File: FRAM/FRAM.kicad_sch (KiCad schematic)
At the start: 4 parts, among them IC1 MB85RC256VPF-G-JNERE2

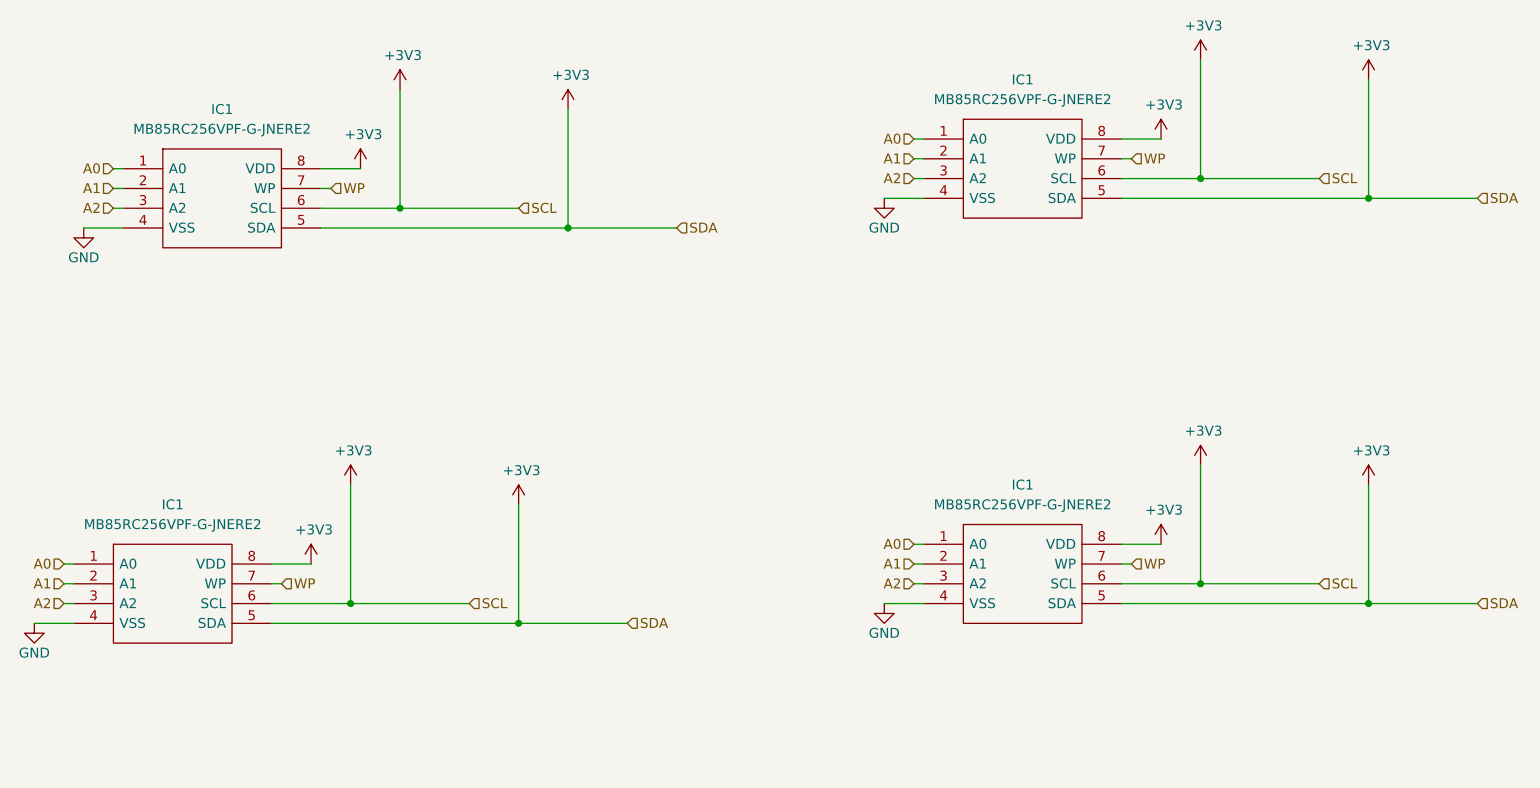
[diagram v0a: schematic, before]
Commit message: Route sensors, IMU and radio board
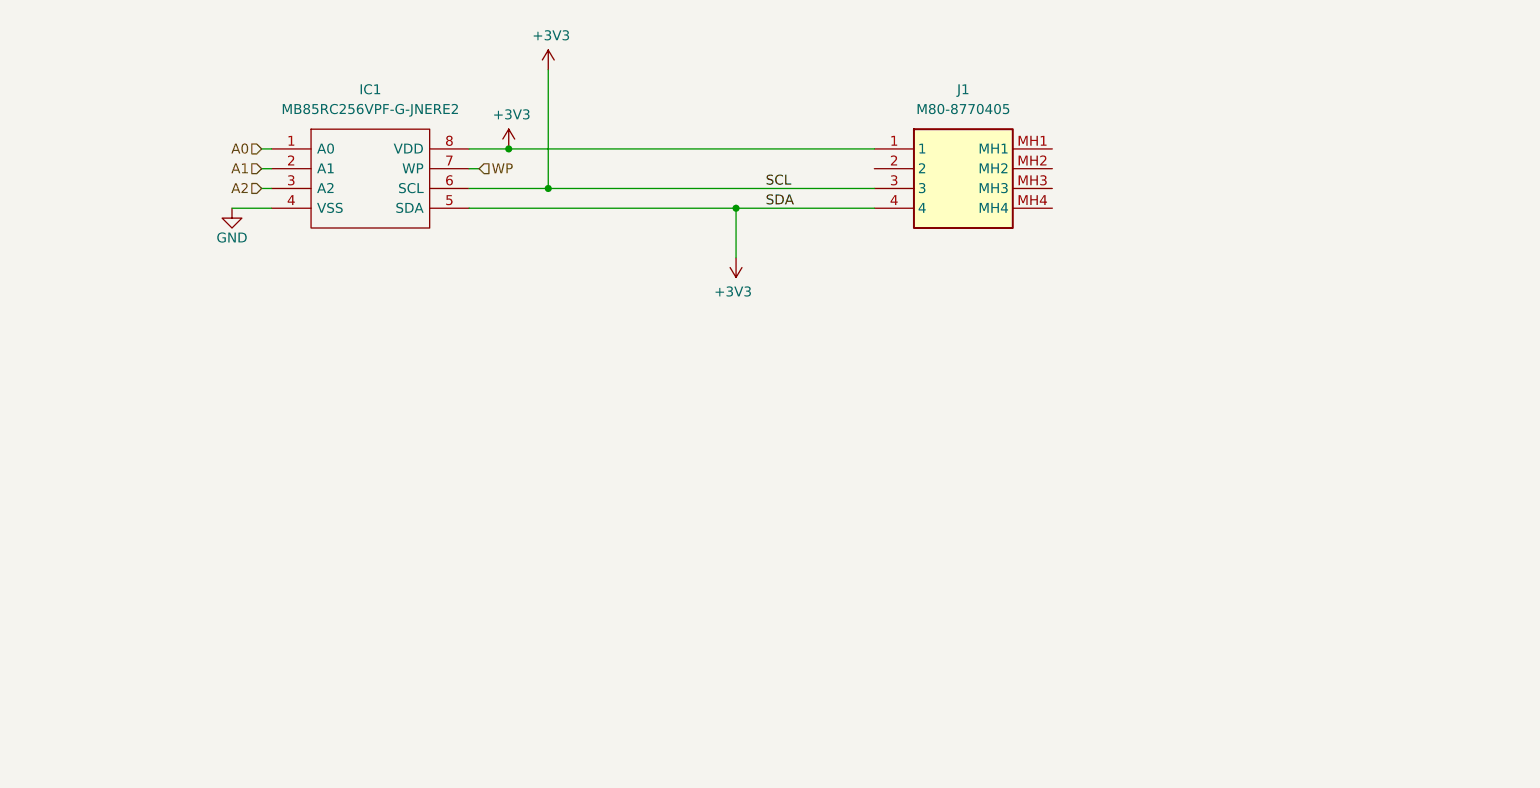
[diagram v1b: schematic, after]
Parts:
- removed IC1 (x3): MB85RC256VPF-G-JNERE2, MB85RC256VPF-G-JNERE2:SOP127P797X210-8N, symbol LibraryLoader:MB85RC256VPF-G-JNERE2
- added J1: M80-8770405, M808770405, symbol M80-8770405:M80-8770405
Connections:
- net +3V3: now also J1.1, J1.3, J1.4
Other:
- moved on the sheet: IC1

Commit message: Done with most of the boards
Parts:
- added R1 (x2): R, Resistor_SMD:R_0603_1608Metric, symbol Device:R
- J1: footprint M808770405 -> KiCad:M808770405
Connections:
- net WP is gone; now on net GND: IC1.7 (WP)
- net +3V3: no longer IC1.5 (SDA), IC1.6 (SCL), J1.3, J1.4
- net GND: now also J1.2
- new net: IC1.6 (SCL), R1.1
- new net SCL: J1.3, R1.2
- new net SDA: IC1.5 (SDA), J1.4, R1.1, R1.2
- no-connect marks 0 -> 4
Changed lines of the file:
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@@
 (kicad_sch (version 20230121) (generator eeschema)
   (paper "A4")
-  (junction (at 147.32 69.85) (diameter 0) (color 0 0 0 0)
-  )
-  (junction (at 123.19 67.31) (diameter 0) (color 0 0 0 0)
+  (junction (at 142.24 69.85) (diameter 0) (color 0 0 0 0)
+  )
+  (junction (at 149.86 69.85) (diameter 0) (color 0 0 0 0)
   )
   (junction (at 118.11 62.23) (diameter 0) (color 0 0 0 0)
   )
+  (junction (at 138.43 64.77) (diameter 0) (color 0 0 0 0)
+  )
+  (no_connect (at 187.96 67.31))
+  (no_connect (at 187.96 64.77))
+  (no_connect (at 187.96 69.85))
+  (no_connect (at 187.96 62.23))
+  (wire (pts (xy 138.43 64.77) (xy 165.1 64.77))
+    (stroke (width 0) (type default))
+  )
   (wire (pts (xy 118.11 62.23) (xy 165.1 62.23))
     (stroke (width 0) (type default))
@@
     (stroke (width 0) (type default))
   )
-  (wire (pts (xy 113.03 64.77) (xy 114.3 64.77))
-    (stroke (width 0) (type default))
-  )
-  (wire (pts (xy 113.03 69.85) (xy 147.32 69.85))
+  (wire (pts (xy 138.43 64.77) (xy 138.43 76.2))
+    (stroke (width 0) (type default))
+  )
+  (wire (pts (xy 113.03 69.85) (xy 142.24 69.85))
     (stroke (width 0) (type default))
   )
@@
     (stroke (width 0) (type default))
   )
+  (wire (pts (xy 86.36 62.23) (xy 87.63 62.23))
+    (stroke (width 0) (type default))
+  )
+  (wire (pts (xy 149.86 69.85) (xy 165.1 69.85))
+    (stroke (width 0) (type default))
+  )
+  (wire (pts (xy 113.03 64.77) (xy 138.43 64.77))
+    (stroke (width 0) (type default))
+  )
+  (wire (pts (xy 130.81 67.31) (xy 165.1 67.31))
+    (stroke (width 0) (type default))
+  )
+  (wire (pts (xy 142.24 69.85) (xy 149.86 69.85))
+    (stroke (width 0) (type default))
+  )
+  (wire (pts (xy 113.03 67.31) (xy 123.19 67.31))
+    (stroke (width 0) (type default))
+  )
+  (wire (pts (xy 86.36 67.31) (xy 87.63 67.31))
+    (stroke (width 0) (type default))
+  )
   (wire (pts (xy 82.55 69.85) (xy 87.63 69.85))
-    (stroke (width 0) (type default))
-  )
-  (wire (pts (xy 123.19 67.31) (xy 165.1 67.31))
-    (stroke (width 0) (type default))
-  )
-  (wire (pts (xy 147.32 69.85) (xy 165.1 69.85))
-    (stroke (width 0) (type default))
-  )
-  (wire (pts (xy 86.36 62.23) (xy 87.63 62.23))
-    (stroke (width 0) (type default))
-  )
-  (wire (pts (xy 123.19 52.07) (xy 123.19 67.31))
-    (stroke (width 0) (type default))
-  )
-  (wire (pts (xy 147.32 69.85) (xy 147.32 76.2))
-    (stroke (width 0) (type default))
-  )
-  (wire (pts (xy 113.03 67.31) (xy 123.19 67.31))
-    (stroke (width 0) (type default))
-  )
-  (wire (pts (xy 86.36 67.31) (xy 87.63 67.31))
     (stroke (width 0) (type default))
   )
@@
   (hierarchical_label "A2" (shape input) (at 86.36 67.31 180) (fields_autoplaced)
     (effects (font (size 1.27 1.27)) (justify right))
-  )
-  (hierarchical_label "WP" (shape input) (at 114.3 64.77 0) (fields_autoplaced)
-    (effects (font (size 1.27 1.27)) (justify left))
   )
   (hierarchical_label "A1" (shape input) (at 86.36 64.77 180) (fields_autoplaced)
@@
     )
   )
-  (symbol (lib_id "power:+3V3") (at 147.32 76.2 180) (unit 1)
+  (symbol (lib_id "power:GND") (at 138.43 76.2 0) (unit 1)
     (in_bom yes) (on_board yes) (dnp no)
-    (property "Reference" "#PWR09" (at 147.32 72.39 0)
-      (effects (font (size 1.27 1.27)) hide)
-    )
-    (property "Value" "+3V3" (at 146.939 80.5942 0)
-      (effects (font (size 1.27 1.27)))
-    )
-    (property "Footprint" "" (at 147.32 76.2 0)
-      (effects (font (size 1.27 1.27)) hide)
-    )
-    (property "Datasheet" "" (at 147.32 76.2 0)
-      (effects (font (size 1.27 1.27)) hide)
-    )
-    (pin "1")
-    (instances
-      (project "STM32F405RGT6-Breakout"
-        (path "/0540e924-c3ed-4064-b360-826f481ae85c"
-          (reference "#PWR09") (unit 1)
-        )
-      )
+    (property "Reference" "#PWR03" (at 138.43 82.55 0)
+      (effects (font (size 1.27 1.27)) hide)
+    )
+    (property "Value" "GND" (at 138.43 80.01 0)
+      (effects (font (size 1.27 1.27)))
+    )
+    (property "Footprint" "" (at 138.43 76.2 0)
+      (effects (font (size 1.27 1.27)) hide)
+    )
+    (property "Datasheet" "" (at 138.43 76.2 0)
+      (effects (font (size 1.27 1.27)) hide)
+    )
+    (pin "1")
+    (instances
       (project "Flight_Computer_V2"
         (path "/39d7ebb3-b69d-4ae9-8f55-c9acfe77d345/4a05f57f-ad7d-4317-b08f-5601038a99f3"
-          (reference "#PWR09") (unit 1)
+          (reference "#PWR03") (unit 1)
         )
         (path "/39d7ebb3-b69d-4ae9-8f55-c9acfe77d345/728ff691-86aa-4406-a714-359017417c15"
-          (reference "#PWR031") (unit 1)
+          (reference "#PWR029") (unit 1)
         )
         (path "/39d7ebb3-b69d-4ae9-8f55-c9acfe77d345/de413d1f-8d39-42d8-b833-6419d9c73587"
-          (reference "#PWR035") (unit 1)
+          (reference "#PWR032") (unit 1)
         )
         (path "/39d7ebb3-b69d-4ae9-8f55-c9acfe77d345/806e3fbd-cca2-40cb-b727-86767e32e959"
-          (reference "#PWR039") (unit 1)
+          (reference "#PWR036") (unit 1)
         )
         (path "/39d7ebb3-b69d-4ae9-8f55-c9acfe77d345/5302a5ff-4c5a-40f5-8b82-1f5be512d366"
-          (reference "#PWR045") (unit 1)
+          (reference "#PWR042") (unit 1)
         )
       )
       (project "STM32F405RGT6"
         (path "/6135eb53-87c0-4516-a6dc-aa2a3e58fdeb"
-          (reference "#PWR02") (unit 1)
-        )
-      )
-      (project "FRAM"
-        (path "/7e9403d5-9e34-459f-9c36-ff767a829e37"
-          (reference "#PWR08") (unit 1)
-        )
-      )
-    )
-  )
-  (symbol (lib_id "power:+3V3") (at 123.19 52.07 0) (unit 1)
-    (in_bom yes) (on_board yes) (dnp no)
-    (property "Reference" "#PWR09" (at 123.19 55.88 0)
-      (effects (font (size 1.27 1.27)) hide)
-    )
-    (property "Value" "+3V3" (at 123.571 47.6758 0)
-      (effects (font (size 1.27 1.27)))
-    )
-    (property "Footprint" "" (at 123.19 52.07 0)
-      (effects (font (size 1.27 1.27)) hide)
-    )
-    (property "Datasheet" "" (at 123.19 52.07 0)
-      (effects (font (size 1.27 1.27)) hide)
-    )
-    (pin "1")
-    (instances
-      (project "STM32F405RGT6-Breakout"
-        (path "/0540e924-c3ed-4064-b360-826f481ae85c"
-          (reference "#PWR09") (unit 1)
-        )
-      )
-      (project "Flight_Computer_V2"
-        (path "/39d7ebb3-b69d-4ae9-8f55-c9acfe77d345/4a05f57f-ad7d-4317-b08f-5601038a99f3"
-          (reference "#PWR09") (unit 1)
-        )
-        (path "/39d7ebb3-b69d-4ae9-8f55-c9acfe77d345/728ff691-86aa-4406-a714-359017417c15"
-          (reference "#PWR015") (unit 1)
-        )
-        (path "/39d7ebb3-b69d-4ae9-8f55-c9acfe77d345/de413d1f-8d39-42d8-b833-6419d9c73587"
-          (reference "#PWR030") (unit 1)
-        )
-        (path "/39d7ebb3-b69d-4ae9-8f55-c9acfe77d345/806e3fbd-cca2-40cb-b727-86767e32e959"
-          (reference "#PWR034") (unit 1)
-        )
-        (path "/39d7ebb3-b69d-4ae9-8f55-c9acfe77d345/5302a5ff-4c5a-40f5-8b82-1f5be512d366"
-          (reference "#PWR038") (unit 1)
-        )
-      )
-      (project "STM32F405RGT6"
-        (path "/6135eb53-87c0-4516-a6dc-aa2a3e58fdeb"
-          (reference "#PWR02") (unit 1)
-        )
-      )
-      (project "FRAM"
-        (path "/7e9403d5-9e34-459f-9c36-ff767a829e37"
-          (reference "#PWR07") (unit 1)
+          (reference "#PWR03") (unit 1)
+        )
+      )
+      (project "FRAM"
+        (path "/7e9403d5-9e34-459f-9c36-ff767a829e37"
+          (reference "#PWR01") (unit 1)
+        )
+      )
+      (project "avionics_flight_computer"
+        (path "/b1d299c5-d712-4abd-abfc-85bf9dc0241e/1d0982b1-a7f8-42e4-83d7-31334d6351d0"
+          (reference "#PWR03") (unit 1)
+        )
+      )
+    )
+  )
+  (symbol (lib_id "Device:R") (at 127 67.31 90) (unit 1)
+    (in_bom yes) (on_board yes) (dnp no) (fields_autoplaced)
+    (property "Reference" "R1" (at 127 60.96 90)
+      (effects (font (size 1.27 1.27)))
+    )
+    (property "Value" "R" (at 127 63.5 90)
+      (effects (font (size 1.27 1.27)))
+    )
+    (property "Footprint" "Resistor_SMD:R_0603_1608Metric" (at 127 69.088 90)
+      (effects (font (size 1.27 1.27)) hide)
+    )
+    (property "Datasheet" "~" (at 127 67.31 0)
+      (effects (font (size 1.27 1.27)) hide)
+    )
+    (pin "1")
+    (pin "2")
+    (instances
+      (project "FRAM"
+        (path "/7e9403d5-9e34-459f-9c36-ff767a829e37"
+          (reference "R1") (unit 1)
+        )
+      )
+    )
+  )
+  (symbol (lib_id "Device:R") (at 146.05 69.85 90) (unit 1)
+    (in_bom yes) (on_board yes) (dnp no) (fields_autoplaced)
+    (property "Reference" "R1" (at 146.05 63.5 90)
+      (effects (font (size 1.27 1.27)))
+    )
+    (property "Value" "R" (at 146.05 66.04 90)
+      (effects (font (size 1.27 1.27)))
+    )
+    (property "Footprint" "Resistor_SMD:R_0603_1608Metric" (at 146.05 71.628 90)
+      (effects (font (size 1.27 1.27)) hide)
+    )
+    (property "Datasheet" "~" (at 146.05 69.85 0)
+      (effects (font (size 1.27 1.27)) hide)
+    )
+    (pin "1")
+    (pin "2")
+    (instances
+      (project "MAGNETOMETER"
+        (path "/1ff82954-21a9-4f7a-99bd-a8202cea8bb4"
+          (reference "R1") (unit 1)
+        )
+      )
+      (project "FRAM"
+        (path "/7e9403d5-9e34-459f-9c36-ff767a829e37"
+          (reference "R2") (unit 1)
         )
       )
@@
       (effects (font (size 1.27 1.27)))
     )
-    (property "Footprint" "M808770405" (at 184.15 157.15 0)
+    (property "Footprint" "KiCad:M808770405" (at 184.15 157.15 0)
       (effects (font (size 1.27 1.27)) (justify left top) hide)
     )

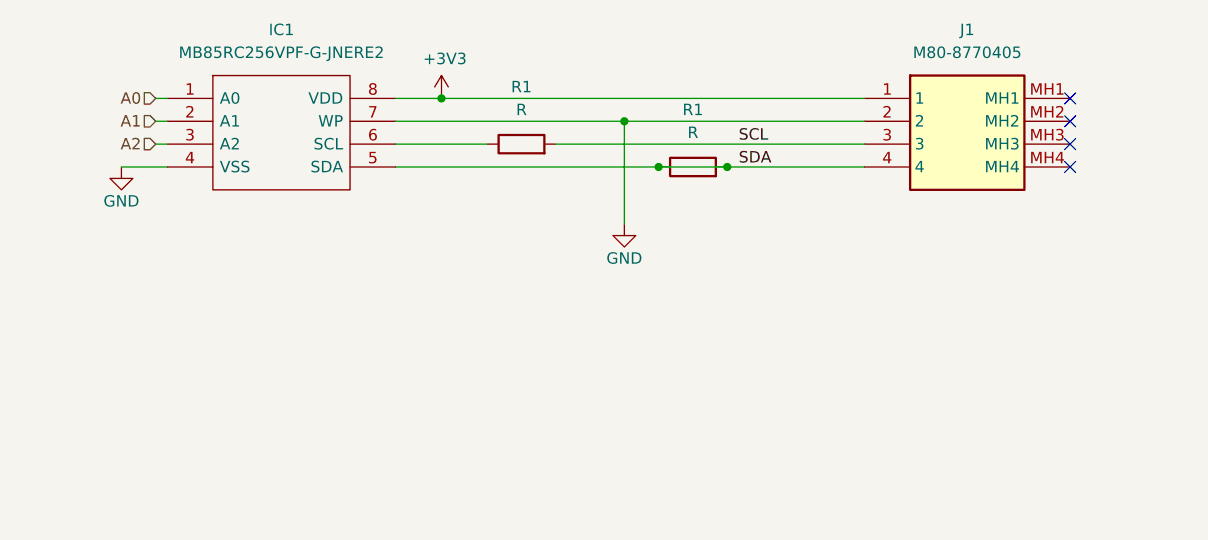
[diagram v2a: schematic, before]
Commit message: Fixed Accel, Barometer, FRAM, Inertia unit, and Magnetometer
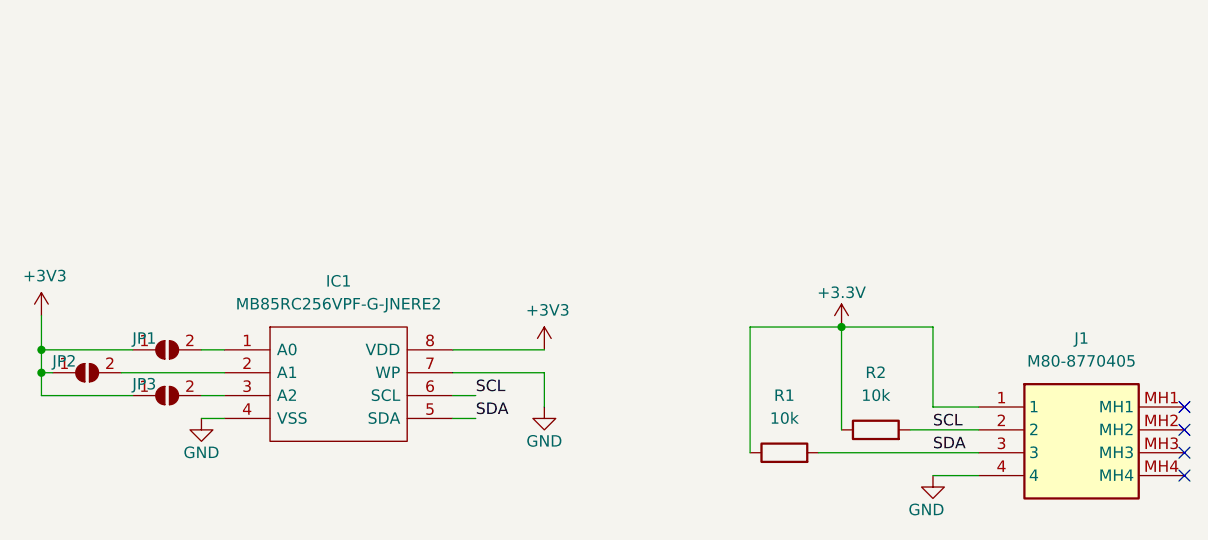
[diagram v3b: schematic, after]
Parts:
- removed R1 (x2): R, Resistor_SMD:R_0603_1608Metric, symbol Device:R
- added JP1, JP2, JP3: SolderJumper_2_Open, Jumper:SolderJumper-2_P1.3mm_Open_RoundedPad1.0x1.5mm, symbol Jumper:SolderJumper_2_Open
- added R1, R2: 10k, Resistor_SMD:R_0201_0603Metric_Pad0.64x0.40mm_HandSolder, symbol Device:R
- J1: footprint KiCad:M808770405 -> M808770405
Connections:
- net +3V3: now also JP1.1 (A), JP2.1 (A), JP3.1 (A); no longer J1.1
- net GND: now also J1.4; no longer J1.2
- net SCL: now also IC1.6 (SCL), J1.2, R2.2; no longer J1.3
- net SDA: now also J1.3, R1.2; no longer J1.4
- net A0: no longer names the net of IC1.1 (A0)
- net A0: now also JP1.2 (B)
- net A1: no longer names the net of IC1.2 (A1)
- net A1: now also JP2.2 (B)
- net A2: no longer names the net of IC1.3 (A2)
- net A2: now also JP3.2 (B)
- new net +3.3V: J1.1, R1.1, R2.1
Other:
- company: (none) -> USST Avionics
- title: (none) -> FRAM
- moved on the sheet: IC1

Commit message: LC24 PCBs
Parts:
- removed J1: M80-8770405, M808770405, symbol M80-8770405:M80-8770405
- added H1, H2, H3, H4: MountingHole_Pad, Mounting_Wuerth:Mounting_Wuerth_WA-SMSI-M1.6_H1mm_9774010633, symbol Mechanical:MountingHole_Pad
- added J2: M80-8770422, Harwin-M80-8770422:CONN_M80-87704_HRW, symbol Harwin-M80-8770422:M80-8770422
- IC1: footprint MB85RC256VPF-G-JNERE2:SOP127P797X210-8N -> FRAM:FPT-8P-M08_FUJ
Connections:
- net +3V3 is gone; now on net +3.3V: IC1.8 (VDD), JP1.1 (A), JP2.1 (A), JP3.1 (A)
- net +3.3V: now also J2.1
- net GND: now also H1.1, H2.1, H3.1, H4.1, J2.4
- net SCL: now also J2.2
- net SDA: now also J2.3
- no-connect marks 4 -> 0
